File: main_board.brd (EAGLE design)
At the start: 100.3 x 69.8 mm, 46 parts, among them P1 ST-TF-003A, U1 STM32F407VGT6, U2 USBLC6-2, U3 MCP1700T-3302E, U4 LTC4054LES5-4.2#TRPBF, X1 MicroUSB-B

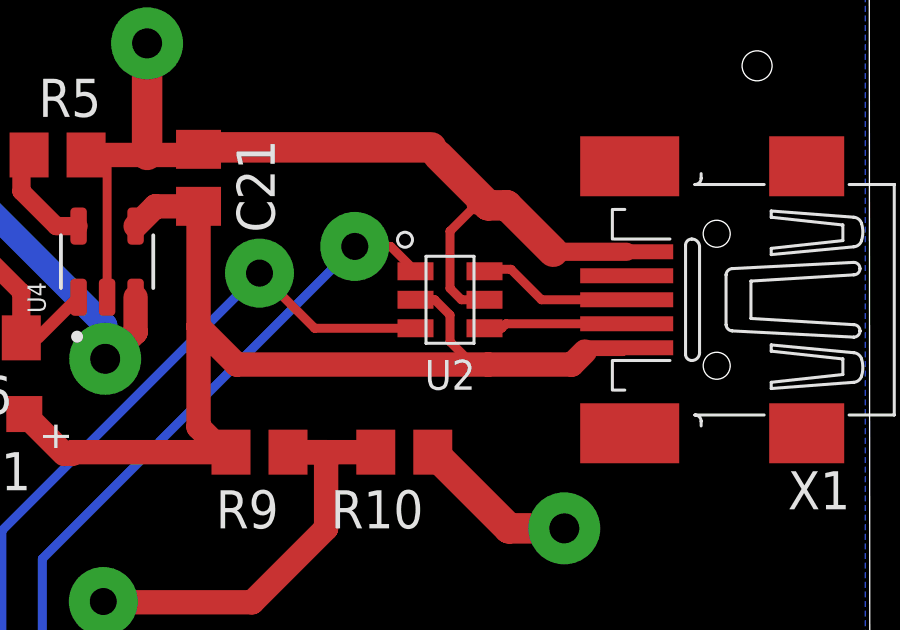
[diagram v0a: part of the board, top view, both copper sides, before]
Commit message: fix scheme error
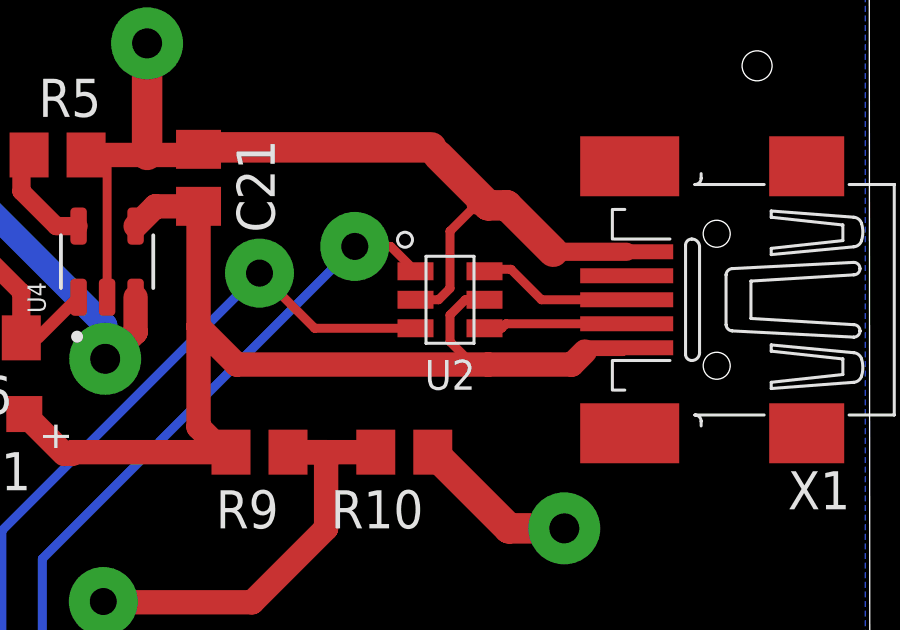
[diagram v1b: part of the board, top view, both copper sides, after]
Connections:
- net +5V: now also U2.P$5; no longer U2.P$2
- net GND: now also U2.P$2; no longer U2.P$5
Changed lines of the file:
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@@
 <wire x1="76.1873" y1="63.0682" x2="77.7138" y2="63.0682" width="0.8128" layer="1"/>
 <wire x1="77.7138" y1="63.0682" x2="77.9018" y2="63.2562" width="0.3" layer="1"/>
-<contactref element="U2" pad="P$5"/>
 <wire x1="88.1761" y1="61.3898" x2="87.5538" y2="61.3898" width="1.016" layer="1"/>
 <wire x1="87.5538" y1="61.3898" x2="87.1454" y2="61.3898" width="0.6096" layer="1"/>
 <wire x1="86.2838" y1="60.5282" x2="86.2838" y2="58.6232" width="0.3" layer="1"/>
-<wire x1="86.2838" y1="58.6232" x2="86.6648" y2="58.2422" width="0.3" layer="1"/>
-<wire x1="86.6648" y1="58.2422" x2="87.4338" y2="58.2422" width="0.3" layer="1"/>
 <wire x1="87.1454" y1="61.3898" x2="86.2838" y2="60.5282" width="0.3" layer="1"/>
 <wire x1="92.1738" y1="59.8422" x2="89.7237" y2="59.8422" width="0.6096" layer="1"/>
@@
 <wire x1="93.9" y1="2.54" x2="88.9" y2="2.54" width="0.8128" layer="1"/>
 <wire x1="87.63" y1="2.54" x2="88.9" y2="2.54" width="0.3" layer="1"/>
+<contactref element="U2" pad="P$2"/>
+<wire x1="86.2838" y1="58.6232" x2="85.9028" y2="58.2422" width="0.3" layer="1"/>
+<wire x1="85.9028" y1="58.2422" x2="85.1338" y2="58.2422" width="0.3" layer="1"/>
 </signal>
 <signal name="I2C_SDA">
@@
 <wire x1="75.8038" y1="60.6972" x2="76.4628" y2="61.3562" width="0.8128" layer="1"/>
 <wire x1="76.4628" y1="61.3562" x2="77.9018" y2="61.3562" width="0.8128" layer="1"/>
-<contactref element="U2" pad="P$2"/>
-<wire x1="85.1338" y1="58.2422" x2="85.7758" y2="58.2422" width="0.3" layer="1"/>
-<wire x1="85.7758" y1="58.2422" x2="86.2838" y2="57.7342" width="0.3" layer="1"/>
-<wire x1="86.2838" y1="57.7342" x2="86.2838" y2="56.8452" width="0.3" layer="1"/>
+<wire x1="86.2838" y1="56.8452" x2="86.2838" y2="57.7342" width="0.3" layer="1"/>
 <wire x1="86.2838" y1="56.8452" x2="87.0458" y2="56.0832" width="0.3" layer="1"/>
 <wire x1="92.0468" y1="56.5152" x2="92.1738" y2="56.6422" width="0.3" layer="1"/>
@@
 <wire x1="77.9018" y1="57.3532" x2="77.9018" y2="54.0004" width="0.8128" layer="1"/>
 <wire x1="77.9018" y1="54.0004" x2="78.74" y2="53.1622" width="0.8128" layer="1"/>
+<contactref element="U2" pad="P$5"/>
+<wire x1="86.2838" y1="57.7342" x2="86.7918" y2="58.2422" width="0.3" layer="1"/>
+<wire x1="86.7918" y1="58.2422" x2="87.4338" y2="58.2422" width="0.3" layer="1"/>
 </signal>
 <signal name="D-">
